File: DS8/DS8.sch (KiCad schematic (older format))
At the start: 168 parts, among them U1 LM358, U2 LM358, U3 LM358, U4 LM358

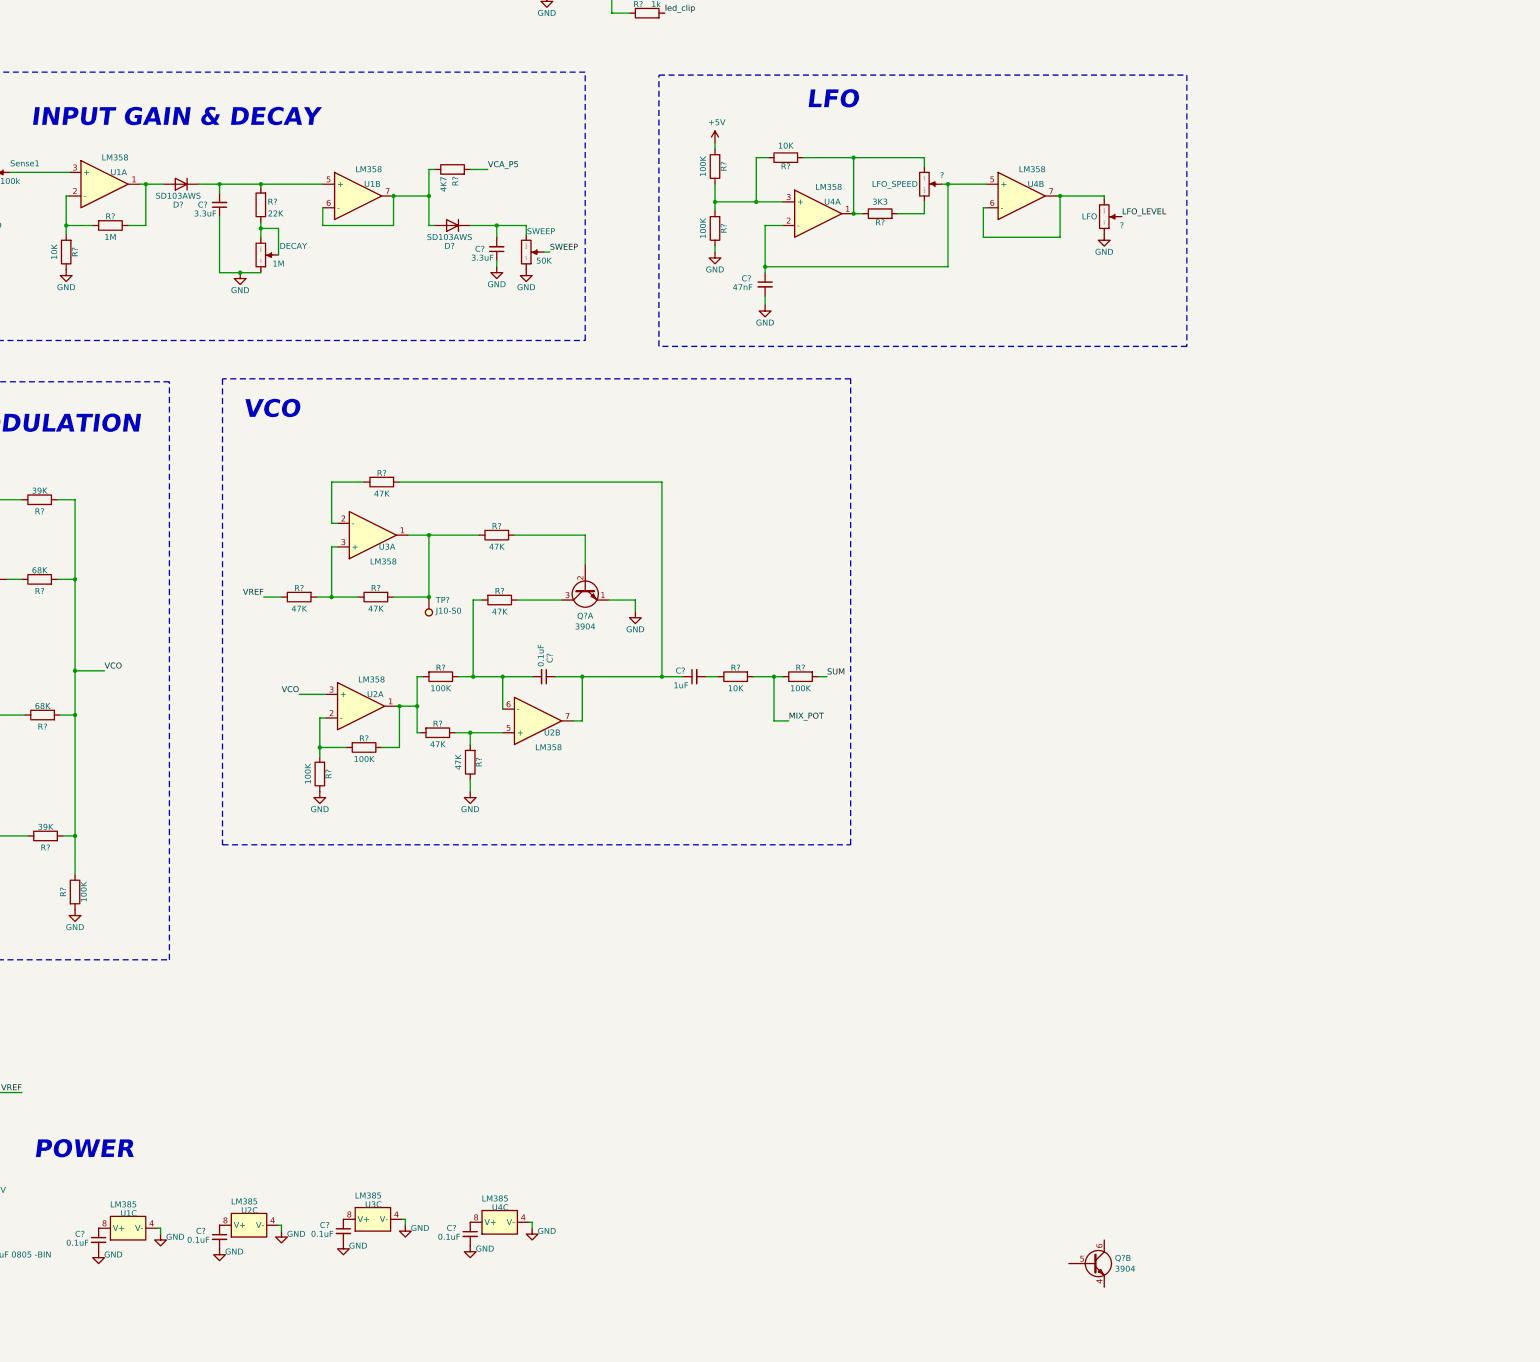
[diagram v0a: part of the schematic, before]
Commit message: DS8 - Added 13700 and Noise chip
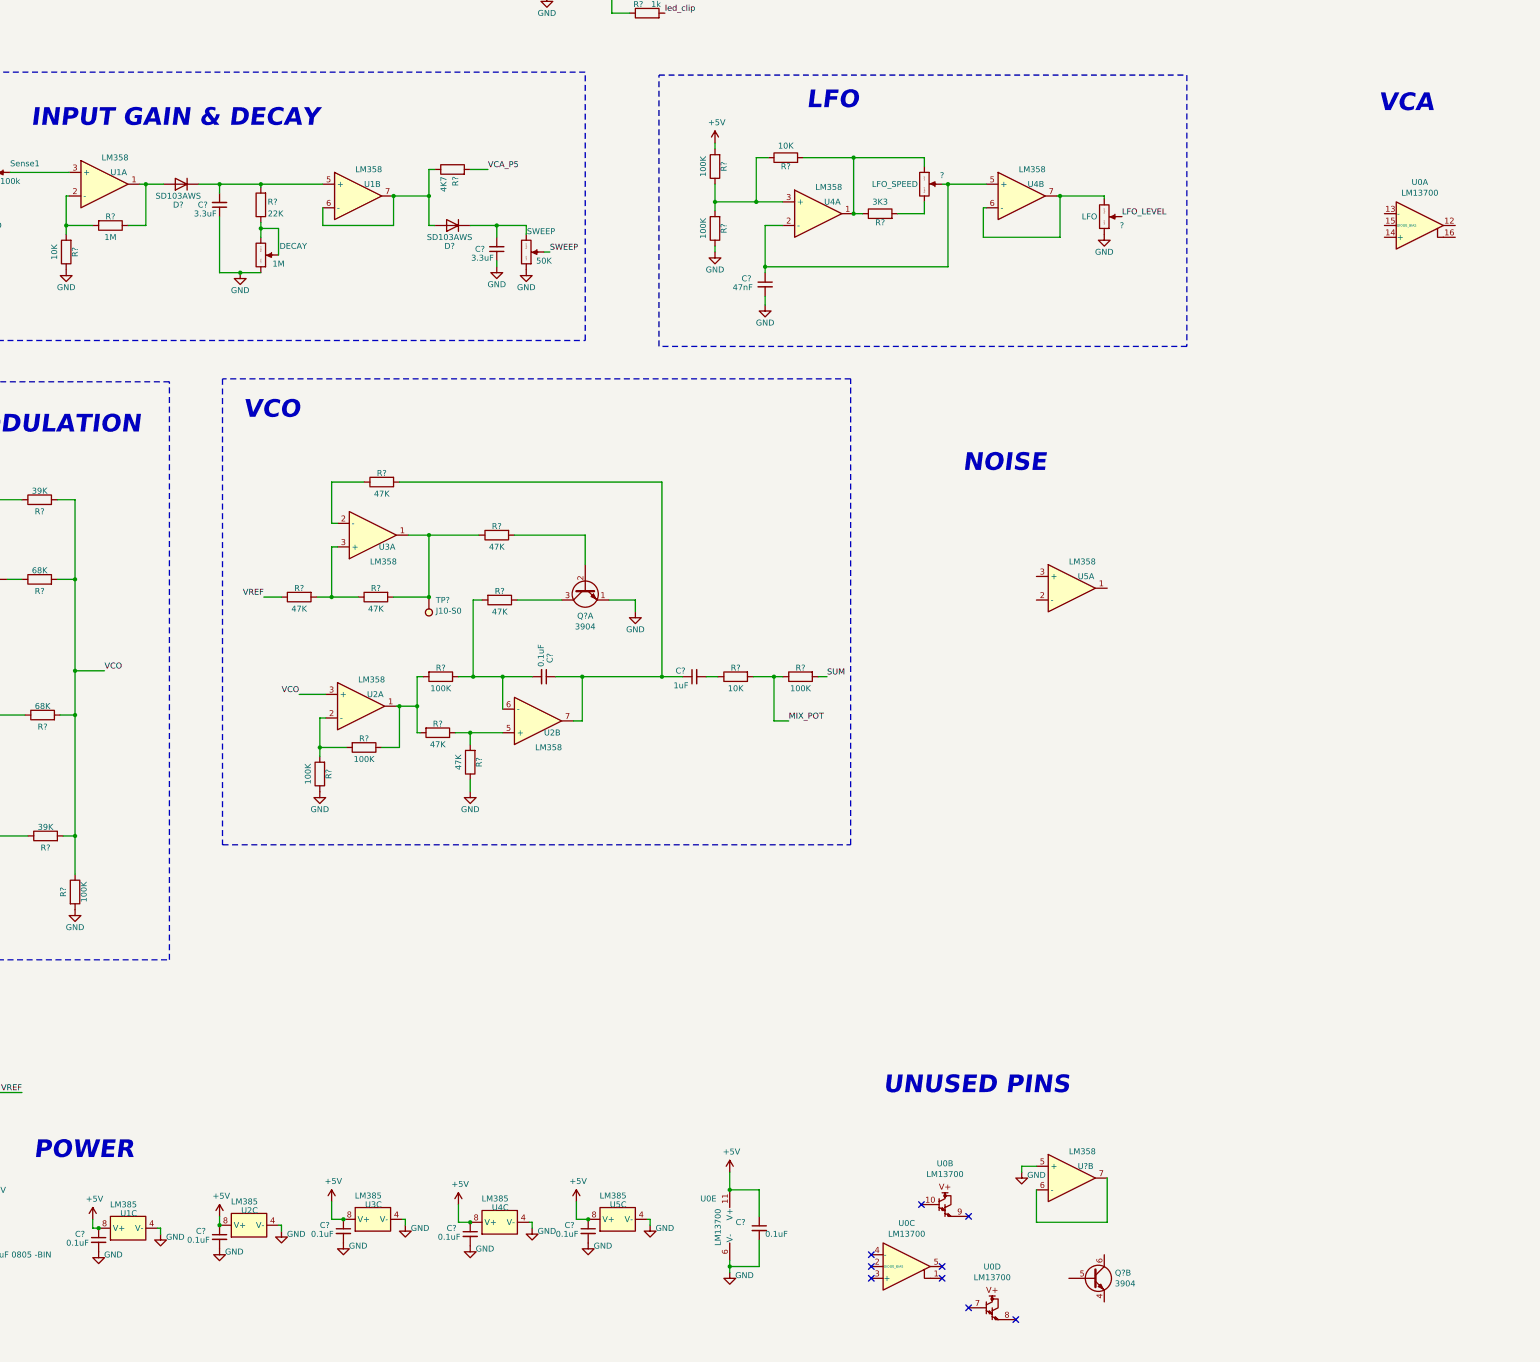
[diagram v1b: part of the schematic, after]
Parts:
- added C? (x2): 0.1uF, 4ms_Capacitor:C_0603, symbol 4ms-passives:C_Small
- added U0: LM13700, symbol 4ms-ic:LM13700
- added U5, U?: LM358, 4ms_Package_SSOP:TSSOP-8_4.4x3mm_Pitch0.65mm, symbol 4ms-ic:NJM2068-separate-power
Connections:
- net +5V: now also C?.1, C?.1, C?.1, C?.1, U1.8 (V+), U2.8 (V+), U3.8 (V+), U4.8 (V+), C?.1, C?.1, U0.11 (V+), U5.8 (V+)
- net GND: now also C?.2, C?.2, U0.6 (V-), U5.4 (V-), U?.5 (+)
- new net: U?.6 (-), U?.7
- no-connect marks 9 -> 18
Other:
- note added: "NOISE"
- note added: "UNUSED PINS"
- note added: "VCA"
- moved on the sheet: Q?B

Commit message: DS8 - Completed schem - about to annotate
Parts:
- removed C?: 22uF, 4ms_Capacitor:C_0805, symbol 4ms-passives:C_Small
- removed C? (x2): 10uF 16v, 4ms_Capacitor:C_0805, symbol 4ms-passives:C_Small
- removed C? (x12): 0.1uF, 4ms_Capacitor:C_0603, symbol 4ms-passives:C_Small
- removed C? (x3): 1uF, 4ms_Capacitor:C_0603, symbol 4ms-passives:C_Small
- removed C? (x2): 220pF, 4ms_Capacitor:C_0603, symbol 4ms-passives:C_Small
- removed C?: 20pF, 4ms_Capacitor:C_0603, symbol 4ms-passives:C_Small
- removed C?: 47uF, 4ms_Capacitor:CP_Elec_5x5.3, symbol 4ms-passives:CP1_Small
- removed C?: 1nF, 4ms_Capacitor:C_0603, symbol 4ms-passives:C_Small
- removed D?: B140HW-7, 4ms_Diode:D_SOD-123, symbol 4ms-passives:B140HW-7
- removed D? (x4): SD103AWS, 4ms_Diode:D_SOD-323F, symbol 4ms-passives:D
- removed D?: BAT54S, 4ms_Package_SOT:SOT23-3_PO132, symbol 4ms-passives:D_Schottky_x2_Serial
- removed ENV_LED?: BLUE, 4ms_LED:LED_0603_1608Metric, symbol 4ms-passives:LED-C1-A2
- removed EnvSense?, Level_?: 100k, 4ms_Potentiometer:Pot_9mm_Knurl_NoDet, symbol 4ms-mech:POT
- removed GATE? (x2), INL?: JACK-MONO, 4ms_Jack:EighthInch_PJ398SM, symbol 4ms-mech:JACK-MONO
- removed GATE_LED?: WHITE, 4ms_LED:LED_0603_1608Metric, symbol 4ms-passives:LED-C1-A2
- removed INV_LED?: GREEN, 4ms_LED:LED_0603_1608Metric, symbol 4ms-passives:LED-C1-A2
- removed J?: Conn_02x04_Odd_Even, 4ms_Connector:Pins_2x04_2.54mm_TH, symbol 4ms-headers:Conn_02x04_Odd_Even
- removed LED?: RGB, 4ms_LED:LED_PLCC-4, symbol 4ms-passives:LED-RGB-CA
- removed Level_?: 100k, 4ms_Potentiometer:Pot_16mm_NoDet_RV16AF-4A, symbol 4ms-mech:POT
- removed Q? (x2): MBT3904DW1, 4ms_Package_SOT:SOT-363_SC-70-6, symbol 4ms-ic:MBT3904DW1
- removed R? (x12): 10k, 4ms_Resistor:R_0603, symbol 4ms-passives:R
- removed R?: 330, 4ms_Resistor:R_0603, symbol 4ms-passives:R
- removed R? (x13): 1k, 4ms_Resistor:R_0603, symbol 4ms-passives:R
- removed R? (x5): 100k, 4ms_Resistor:R_0603, symbol 4ms-passives:R
- removed R? (x2): 47k, 4ms_Resistor:R_0603, symbol 4ms-passives:R
- removed R?: 22k, 4ms_Resistor:R_0603, symbol 4ms-passives:R
- removed R?: 2k, 4ms_Resistor:R_0603, symbol 4ms-passives:R
- removed R?: 49k9, 4ms_Resistor:R_0603, symbol 4ms-passives:R
- removed R?: 4k7, 4ms_Resistor:R_0603, symbol 4ms-passives:R
- removed R?: 13k, 4ms_Resistor:R_0603, symbol 4ms-passives:R
- removed R? (x2): 1M, 4ms_Resistor:R_0603, symbol 4ms-passives:R
- removed R?: 6k04, 4ms_Resistor:R_0603, symbol 4ms-passives:R
- removed R?: 100R, 4ms_Resistor:R_0603, symbol 4ms-passives:R
- removed R?: 20k, 4ms_Resistor:R_0603, symbol 4ms-passives:R
- removed TR?: 100k, 4ms_Potentiometer:Pot_Trim_SMT_TC33X, symbol 4ms-mech:TRIMPOT
- removed U? (x12): TL082, 4ms_Package_SSOP:TSSOP-8_4.4x3mm_Pitch0.65mm, symbol 4ms-ic:NJM2068-separate-power
- removed U? (x5): CD4001, 4ms_Package_SOIC:SOIC-14_3.9x8.65mm_Pitch1.27mm, symbol 4ms-ic:4001
- removed U? (x3): NJM2068, 4ms_Package_SSOP:TSSOP-8_4.4x3mm_Pitch0.65mm, symbol 4ms-ic:NJM2068-separate-power
- added C?: 22pF, 4ms_Capacitor:C_0603, symbol 4ms-passives:C_Small
- added C? (x2): 10nF, 4ms_Capacitor:C_0603, symbol 4ms-passives:C_Small
- added C?: 4.7nF, 4ms_Capacitor:C_0603, symbol 4ms-passives:C_Small
- added C?: 1nF, 4ms_Capacitor:C_0603, symbol 4ms-passives:C_Small
- added C?: 47nF, 4ms_Capacitor:C_0603, symbol 4ms-passives:C_Small
- added C? (x2): 1uF, 4ms_Capacitor:C_0805, symbol 4ms-passives:C_Small
- added DCJack, OUT: JACK-MONO, 4ms_Jack:EighthInch_PJ398SM, symbol 4ms-mech:JACK-MONO
- added Mix: ?, 4ms_Potentiometer:Pot_16mm_NoDet_RV16AF-4A, symbol 4ms-mech:POT
- added Q? (x2): 3904, 4ms-footprints:TO-92_Molded_Narrow, symbol 4ms-passives:Dual_Transistor
- added R? (x2): 100K, 4ms_Resistor:R_0603, symbol 4ms-passives:R
- added R?: 470K, 4ms_Resistor:R_0603, symbol 4ms-passives:R
- added R?: 1M, 4ms_Resistor:R_0603, symbol 4ms-passives:R
- added R?: 330R, 4ms_Resistor:R_0603, symbol 4ms-passives:R
- added R?: 15K, 4ms_Resistor:R_0603, symbol 4ms-passives:R
- added R? (x2): 10K, 4ms_Resistor:R_0603, symbol 4ms-passives:R
- added R?: 33K, 4ms_Resistor:R_0603, symbol 4ms-passives:R
- added R? (x2): 220R, 4ms_Resistor:R_0603, symbol 4ms-passives:R
- added R?: NC, 4ms_Resistor:R_0603, symbol 4ms-passives:R
- gave numbers to parts that had none: 2
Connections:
- net +5V: now also R?.1, R?.2
- net GND: now also C?.2, C?.2, DCJack.2 (SHEILD), Mix.2 (Center), OUT.2 (SHEILD), Q?.2 (B), Q?.4 (E), R?.1
- net SUM: now also C?.1, R?.2
- net VCA_P5: now also U0.1
- net VREF: now also R?.1, R?.1, R?.1
- net at P?.1 (+12V), P?.2 (+12V): now also DCJack.3 (SW); no longer D?.2 (A)
- net at P?.10 (-12V): no longer P?.9 (-12V)
- net at SEL_NOISE.2 (B): now also U5.2 (-), C?.2, R?.1
- net at U5.1: now also C?.1, C?.2, R?.2
- net at U5.3 (+): now also C?.1, R?.2
- net +12V: no longer names the net of C?.1, D?.1 (K)
- net +9V: no longer names the net of C?.1, U?.3 (IN)
- net MIX_POT renamed MIX_POT_1
- net MIX_POT_1: now also Mix.1 (Left)
- net audio_to_switch: no longer names the net of SEL_NOISE.3 (C)
- net audio_to_switch: now also C?.1
- net clock_to_switch: no longer names the net of SEL_NOISE.1 (A)
- net clock_to_switch: now also C?.1
- new net: C?.2, R?.2, U0.3 (+)
- new net: R?.1, R?.2, R?.2, U0.4 (-)
- new net: C?.1, R?.2, U0.5
- new net: D?.2 (A), DCJack.1 (SIG)
- new net: C?.2, Q?.6 (C), R?.1, R?.2
- new net: C?.1, Q?.5 (B), R?.1
- new net: C?.2, Q?.1 (E), R?.2
- new net: C?.1, R?.1
- new net: C?.2, R?.1
- new net: OUT.1 (SIG), R?.2
- new net MIX_POT_3: Mix.3 (Right), R?.1, R?.2
- no-connect marks 18 -> 15
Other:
- note added: "MIX/PAN POT"
- note removed: "AUDIO OUT\nGAIN (x2)"
- note removed: "ENVELOPES"
- note removed: "EXPANDER \nHEADER"
- note removed: "INPUT CLIP"
- note removed: "ONE-SHOT/GATE"
- note removed: "SPDT on\nExpander"
- note removed: "\n"
- note removed: "max gain"
- note removed: "no gain"
- moved on the sheet: C?, D?, P?, Q?B, R?, SEL_NOISEA, U0B, U0D, U0E, U1C, U2C, U3B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

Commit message: placing pcb parts
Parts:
- added POWER1: ON/ON, 4ms_Switch:Switch_Toggle_SPDT_SubMini, symbol 4ms-mech:SW_SPDT
- added Piezo1: JACK-MONO, 4ms_Jack:EighthInch_PJ398SM, symbol 4ms-mech:JACK-MONO
- added Volume1: 100K, 4ms_Potentiometer:Pot_16mm_NoDet_RV16AF-4A, symbol 4ms-mech:POT
- LFO1: renamed from LFO; value ? -> 2M2
- Mix1: renamed from Mix; value ? -> 50K-100K
- PITCH1: renamed from PITCH; value 100K -> 50K
- Q1, Q2: renamed from Q?; footprint 4ms-footprints:TO-92_Molded_Narrow -> 4ms_Package_SOT:SOT-363_SC-70-6; symbol 4ms-passives:Dual_Transistor -> 4ms-ic:MBT3904DW1
- SEL_NOISE1: renamed from SEL_NOISE; footprint 4ms_Switch:Slide_Switch_Runrun_SS22D06 -> 4ms_Switch:Switch_Toggle_SPDT_SubMini; symbol 4ms-mech:DPDT-shielded-sep -> 4ms-mech:SW_SPDT
- Sense1: value 100k -> 50kA
- TP1: renamed from TP?; footprint (none) -> 4ms_TestPoint:TestPoint_WireHole
- U0: footprint (none) -> 4ms_Package_SOIC:SOIC-16_3.9x9.9mm_Pitch1.27mm
- U1, U2, U3, U4, U5: value LM358 -> LM385
- gave numbers to parts that had none: 68
- renumbered CV_In to CV_In1, DCJack to DCJack1, DECAY to DECAY1, LFO_SPEED to LFO_SPEED1, OUT to OUT1, SWEEP to SWEEP1, Trigger_In to Trigger_In1
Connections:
- net GND: now also Piezo1.2 (SHEILD), Volume1.1 (Left); no longer Trigger_In1.3 (SW)
- net at R3.2, U0.5: now also Volume1.3 (Right); no longer C2.1
- net at D3.2 (A): now also POWER1.2; no longer DCJack1.1 (SIG)
- net at C10.2, R25.1, R26.2: now also Q1.3 (C2); no longer Q1.6 (C)
- net at R24.1: now also Q1.6 (C1); no longer Q1.3 (C)
- new net: Piezo1.1 (SIG), Trigger_In1.3 (SW)
- new net: C2.1, Volume1.2 (Center)
- new net: DCJack1.1 (SIG), POWER1.1
- no-connect marks 15 -> 17
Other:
- note added: "INCOMING POWER"
- moved on the sheet: C14, C2, C7, C8, D3, DCJack1, OUT1, P1, R11, SEL_NOISE1

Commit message: continued work on pcb
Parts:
- renumbered Q2 to Q1, Q1 to Q2
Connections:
- no-connect marks 17 -> 20
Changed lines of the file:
@@
 $EndComp
 $Comp
-L 4ms-ic:MBT3904DW1 Q2
+L 4ms-ic:MBT3904DW1 Q1
 U 2 1 5ED790AC
 P 15450 9525
-F 0 "Q2" H 15640 9571 50  0000 L CNN
+F 0 "Q1" H 15640 9571 50  0000 L CNN
 F 1 "3904" H 15640 9480 50  0000 L CNN
 F 2 "4ms_Package_SOT:SOT-363_SC-70-6" H 15650 9450 50  0001 L CIN
@@
 $EndComp
 $Comp
-L 4ms-ic:MBT3904DW1 Q1
+L 4ms-ic:MBT3904DW1 Q2
 U 2 1 5E450D15
 P 11000 5775
-F 0 "Q1" H 11190 5821 50  0000 L CNN
+F 0 "Q2" H 11190 5821 50  0000 L CNN
 F 1 "3904" H 11190 5730 50  0000 L CNN
 F 2 "4ms_Package_SOT:SOT-363_SC-70-6" H 11200 5700 50  0001 L CIN
@@
 Text Notes 9100 8250 0    150  Italic 30
 INCOMING POWER
+NoConn ~ 15550 9325
+NoConn ~ 15550 9725
+NoConn ~ 15250 9525
 $EndSCHEMATC
